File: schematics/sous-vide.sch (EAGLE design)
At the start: 31 parts, among them IC1 MEGA8-P, T1 BC547, T2 BC547, T3 BC547

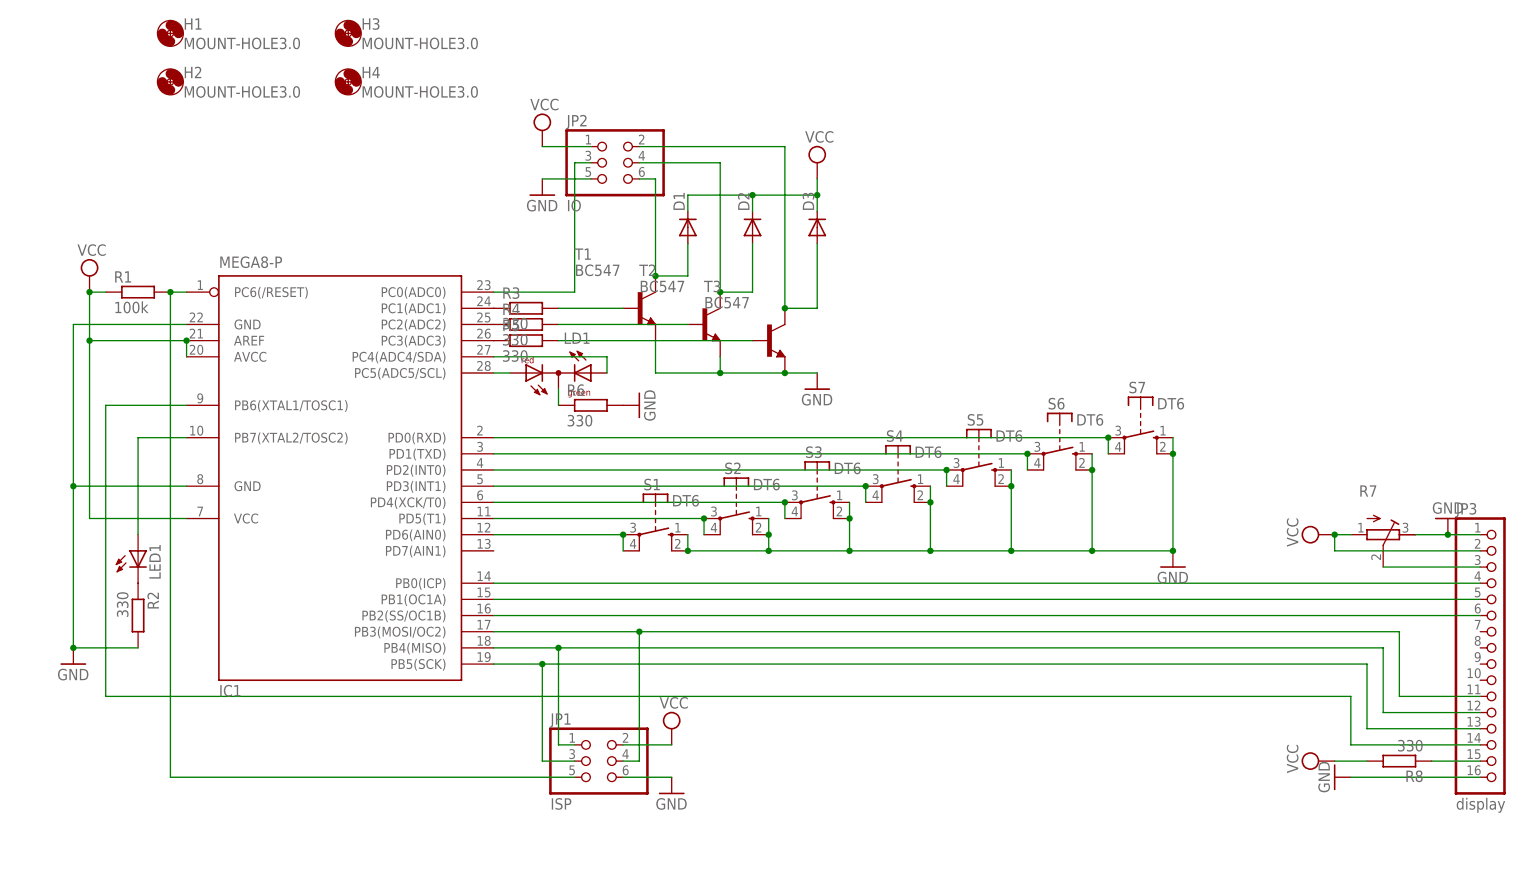
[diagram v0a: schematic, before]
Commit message: Reworked schema and pcb for new buttons and display.
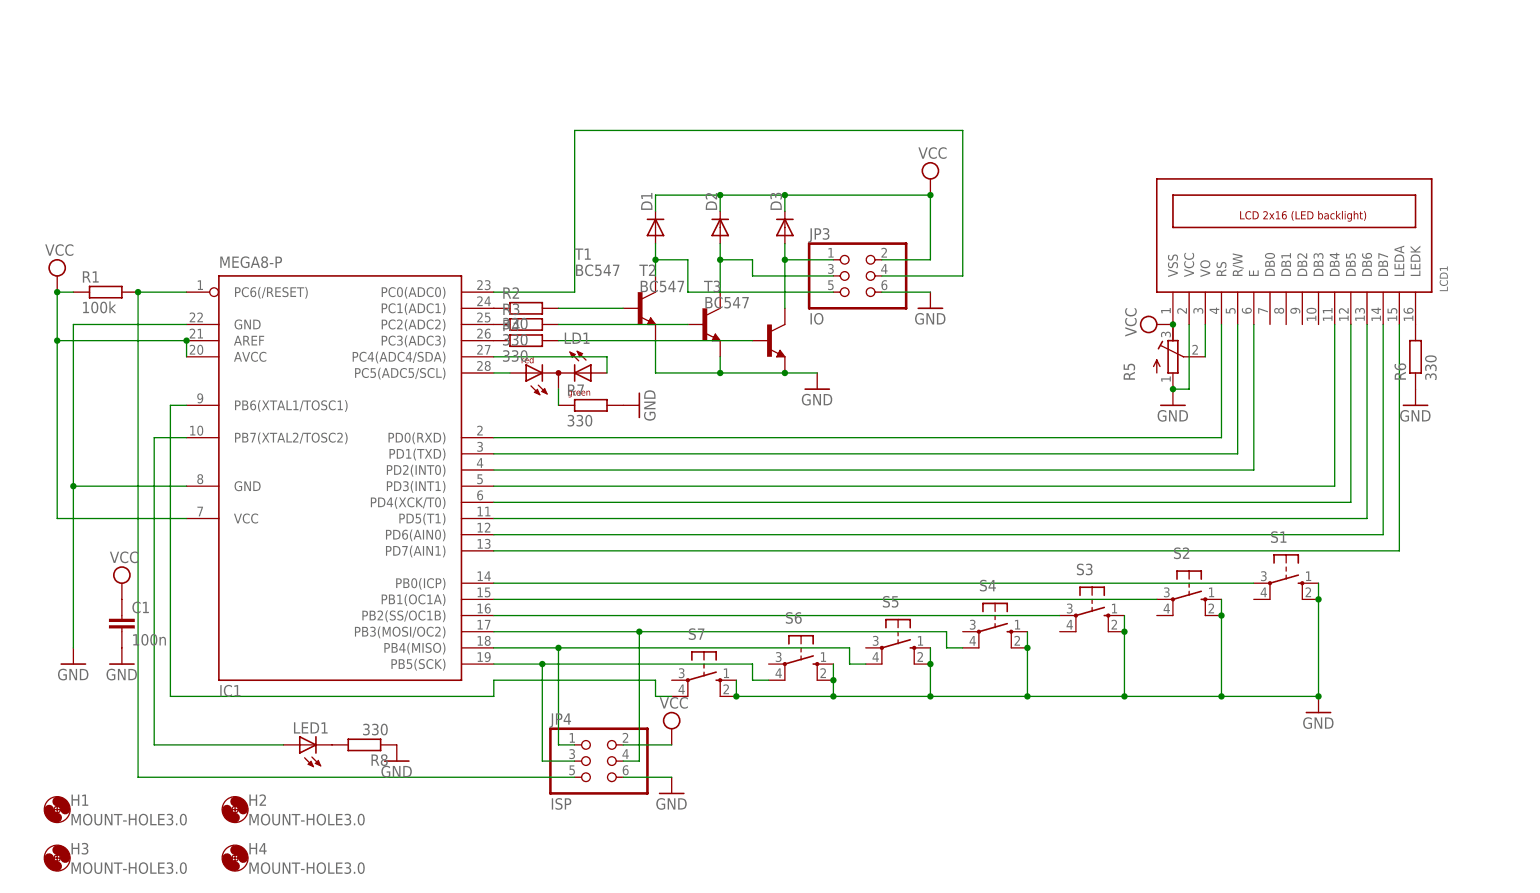
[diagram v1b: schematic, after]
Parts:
- removed JP2: IO, pinhead:PINHD-2X3
- added C1: 100n, resistor:C-EU025-025X050
- added LCD1: LCD_2X16_SIL, lcd_2x16_led_backlight:LCD_2X16_SIL
- JP3: value display -> IO; device pinhead:PINHD-1X16 -> pinhead:PINHD-2X3
- R5: value 330 -> (none); device rcl:R-EU_0207/2V -> resistor:R-TRIMM3339P
- R7: value (none) -> 330; device resistor:R-TRIMM3339P -> rcl:R-EU_0207/2V
- S1, S2, S3, S4, S5, S6, S7: value DT6 -> (none); device switch-misc:DT6 -> switch-omron:40-XX
- renumbered JP1 to JP4
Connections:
- removed net N$15 (its old number): JP3.15, R8.1
- removed net N$20: IC1.PB0(ICP), JP3.4
- new net N$2: LCD1.LEDK, R6.2
- new net N$33: IC1.PD6(AIN0), LCD1.DB7
- new net N$34: IC1.PD7(AIN1), LCD1.LEDA
- net GND: now also C1.2, JP3.6, LCD1.VCC, R5.E, R6.1, R7.2, R8.1, S1.S1, S2.S1, S3.S1, S4.S1, S5.S1, S6.S1, S7.S1; no longer JP2.5, JP3.1, JP3.16, R2.2, R6.2, R7.A, S1.S@1, S2.S@1, S3.S@1, S4.S@1, S5.S@1, S6.S@1, S7.S@1
- net N$1: now also R8.2; no longer R2.1
- net N$10: now also R2.2; no longer R3.2
- net N$11: now also R3.2; no longer R4.2
- net N$12: now also R4.2; no longer R5.2
- net N$13: now also JP3.5; no longer JP2.6
- net N$14: now also LCD1.VO, R5.S; no longer JP3.3, R7.S
- net N$16: now also JP3.3; no longer JP2.4
- net N$17: now also JP3.1; no longer JP2.2
- net N$18: now also S6.P1; no longer JP3.13
- net N$19: now also S5.P1; no longer JP3.12
- net N$21: now also IC1.PD0(RXD), LCD1.RS; no longer IC1.PB1(OC1A), JP3.5
- net N$22: now also IC1.PD1(TXD), LCD1.R/W; no longer IC1.PB2(SS/OC1B), JP3.6
- net N$23: now also IC1.PD2(INT0), LCD1.E; no longer IC1.PB6(XTAL1/TOSC1), JP3.14
- net N$24: now also S4.P1; no longer JP3.11
- net N$26: now also IC1.PB6(XTAL1/TOSC1), S7.P1; no longer IC1.PD6(AIN0), S1.P, S1.P@1
- net N$28: now also IC1.PD3(INT1), LCD1.DB4; no longer IC1.PD5(T1), S2.P, S2.P@1
- net N$3: now also JP3.4; no longer JP2.3
- net N$30: now also IC1.PD4(XCK/T0), LCD1.DB5; no longer IC1.PD3(INT1), S4.P, S4.P@1
- net N$32: now also IC1.PD5(T1), LCD1.DB6; no longer IC1.PD4(XCK/T0), S3.P, S3.P@1
- net N$35: now also IC1.PB2(SS/OC1B), S3.P; no longer IC1.PD2(INT0), S5.P, S5.P@1
- net N$36: now also IC1.PB0(ICP), S1.P; no longer IC1.PD0(RXD), S7.P, S7.P@1
- net N$37: now also IC1.PB1(OC1A), S2.P; no longer IC1.PD1(TXD), S6.P, S6.P@1
- net N$4: now also R2.1; no longer R3.1
- net N$5: now also R3.1; no longer R4.1
- net N$6: now also R4.1; no longer R5.1
- net N$7: now also R7.1; no longer R6.1
- net VCC: now also C1.1, LCD1.VSS, R5.A; no longer JP2.1, R7.E, R8.2
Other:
- moved on the sheet: D1, D2, D3, H1, H2, H3, H4, LED1, R1, R2, R3, R4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

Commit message: Minor tweaks before shipping to pcb manufacturer.
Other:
- moved on the sheet: LCD1, R5, R6
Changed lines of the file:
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@@
 <instance part="GND7" gate="1" x="5.08" y="33.02"/>
 <instance part="R7" gate="G$1" x="86.36" y="73.66"/>
-<instance part="GND5" gate="1" x="177.8" y="73.66"/>
-<instance part="R5" gate="G$1" x="177.8" y="81.28"/>
-<instance part="R6" gate="G$1" x="215.9" y="81.28" rot="R90"/>
-<instance part="SUPPLY4" gate="G$1" x="175.26" y="86.36" rot="R90"/>
-<instance part="GND6" gate="1" x="215.9" y="73.66"/>
+<instance part="GND5" gate="1" x="160.02" y="73.66"/>
+<instance part="R5" gate="G$1" x="160.02" y="81.28"/>
+<instance part="R6" gate="G$1" x="198.12" y="81.28" rot="R90"/>
+<instance part="SUPPLY4" gate="G$1" x="157.48" y="86.36" rot="R90"/>
+<instance part="GND6" gate="1" x="198.12" y="73.66"/>
 <instance part="H1" gate="G$1" x="2.54" y="10.16"/>
 <instance part="H3" gate="G$1" x="2.54" y="2.54"/>
@@
 <instance part="R4" gate="G$1" x="76.2" y="83.82"/>
 <instance part="JP3" gate="A" x="127" y="93.98"/>
-<instance part="LCD1" gate="G$1" x="177.8" y="99.06" rot="R90"/>
+<instance part="LCD1" gate="G$1" x="160.02" y="99.06" rot="R90"/>
 <instance part="GND9" gate="1" x="55.88" y="17.78"/>
 <instance part="S7" gate="1" x="104.14" y="30.48" rot="R270"/>
@@
 <pinref part="GND5" gate="1" pin="GND"/>
 <pinref part="LCD1" gate="G$1" pin="VCC"/>
-<wire x1="180.34" y1="86.36" x2="180.34" y2="76.2" width="0.1524" layer="91"/>
-<wire x1="180.34" y1="76.2" x2="177.8" y2="76.2" width="0.1524" layer="91"/>
-<junction x="177.8" y="76.2"/>
+<wire x1="162.56" y1="86.36" x2="162.56" y2="76.2" width="0.1524" layer="91"/>
+<wire x1="162.56" y1="76.2" x2="160.02" y2="76.2" width="0.1524" layer="91"/>
+<junction x="160.02" y="76.2"/>
 </segment>
 <segment>
@@
 <pinref part="SUPPLY4" gate="G$1" pin="VCC"/>
 <pinref part="R5" gate="G$1" pin="A"/>
-<junction x="177.8" y="86.36"/>
+<junction x="160.02" y="86.36"/>
 </segment>
 <segment>
@@
 <pinref part="IC1" gate="G$1" pin="PD0(RXD)"/>
 <pinref part="LCD1" gate="G$1" pin="RS"/>
-<wire x1="71.12" y1="68.58" x2="185.42" y2="68.58" width="0.1524" layer="91"/>
-<wire x1="185.42" y1="68.58" x2="185.42" y2="86.36" width="0.1524" layer="91"/>
+<wire x1="71.12" y1="68.58" x2="167.64" y2="68.58" width="0.1524" layer="91"/>
+<wire x1="167.64" y1="68.58" x2="167.64" y2="86.36" width="0.1524" layer="91"/>
 </segment>
 </net>
@@
 <pinref part="IC1" gate="G$1" pin="PD1(TXD)"/>
 <pinref part="LCD1" gate="G$1" pin="R/W"/>
-<wire x1="71.12" y1="66.04" x2="187.96" y2="66.04" width="0.1524" layer="91"/>
-<wire x1="187.96" y1="66.04" x2="187.96" y2="86.36" width="0.1524" layer="91"/>
+<wire x1="71.12" y1="66.04" x2="170.18" y2="66.04" width="0.1524" layer="91"/>
+<wire x1="170.18" y1="66.04" x2="170.18" y2="86.36" width="0.1524" layer="91"/>
 </segment>
 </net>
@@
 <pinref part="IC1" gate="G$1" pin="PD2(INT0)"/>
 <pinref part="LCD1" gate="G$1" pin="E"/>
-<wire x1="71.12" y1="63.5" x2="190.5" y2="63.5" width="0.1524" layer="91"/>
-<wire x1="190.5" y1="63.5" x2="190.5" y2="86.36" width="0.1524" layer="91"/>
+<wire x1="71.12" y1="63.5" x2="172.72" y2="63.5" width="0.1524" layer="91"/>
+<wire x1="172.72" y1="63.5" x2="172.72" y2="86.36" width="0.1524" layer="91"/>
 </segment>
 </net>
@@
 <segment>
 <pinref part="IC1" gate="G$1" pin="PD3(INT1)"/>
-<wire x1="71.12" y1="60.96" x2="203.2" y2="60.96" width="0.1524" layer="91"/>
+<wire x1="71.12" y1="60.96" x2="185.42" y2="60.96" width="0.1524" layer="91"/>
 <pinref part="LCD1" gate="G$1" pin="DB4"/>
-<wire x1="203.2" y1="60.96" x2="203.2" y2="86.36" width="0.1524" layer="91"/>
+<wire x1="185.42" y1="60.96" x2="185.42" y2="86.36" width="0.1524" layer="91"/>
 </segment>
 </net>
@@
 <segment>
 <pinref part="IC1" gate="G$1" pin="PD4(XCK/T0)"/>
-<wire x1="71.12" y1="58.42" x2="205.74" y2="58.42" width="0.1524" layer="91"/>
+<wire x1="71.12" y1="58.42" x2="187.96" y2="58.42" width="0.1524" layer="91"/>
 <pinref part="LCD1" gate="G$1" pin="DB5"/>
-<wire x1="205.74" y1="58.42" x2="205.74" y2="86.36" width="0.1524" layer="91"/>
+<wire x1="187.96" y1="58.42" x2="187.96" y2="86.36" width="0.1524" layer="91"/>
 </segment>
 </net>
@@
 <segment>
 <pinref part="IC1" gate="G$1" pin="PD5(T1)"/>
-<wire x1="71.12" y1="55.88" x2="208.28" y2="55.88" width="0.1524" layer="91"/>
+<wire x1="71.12" y1="55.88" x2="190.5" y2="55.88" width="0.1524" layer="91"/>
 <pinref part="LCD1" gate="G$1" pin="DB6"/>
-<wire x1="208.28" y1="55.88" x2="208.28" y2="86.36" width="0.1524" layer="91"/>
+<wire x1="190.5" y1="55.88" x2="190.5" y2="86.36" width="0.1524" layer="91"/>
 </segment>
 </net>
@@
 <segment>
 <pinref part="IC1" gate="G$1" pin="PD6(AIN0)"/>
-<wire x1="71.12" y1="53.34" x2="210.82" y2="53.34" width="0.1524" layer="91"/>
+<wire x1="71.12" y1="53.34" x2="193.04" y2="53.34" width="0.1524" layer="91"/>
 <pinref part="LCD1" gate="G$1" pin="DB7"/>
-<wire x1="210.82" y1="86.36" x2="210.82" y2="53.34" width="0.1524" layer="91"/>
+<wire x1="193.04" y1="86.36" x2="193.04" y2="53.34" width="0.1524" layer="91"/>
 </segment>
 </net>
@@
 <pinref part="IC1" gate="G$1" pin="PD7(AIN1)"/>
 <pinref part="LCD1" gate="G$1" pin="LEDA"/>
-<wire x1="71.12" y1="50.8" x2="213.36" y2="50.8" width="0.1524" layer="91"/>
-<wire x1="213.36" y1="50.8" x2="213.36" y2="86.36" width="0.1524" layer="91"/>
+<wire x1="71.12" y1="50.8" x2="195.58" y2="50.8" width="0.1524" layer="91"/>
+<wire x1="195.58" y1="50.8" x2="195.58" y2="86.36" width="0.1524" layer="91"/>
 </segment>
 </net>
@@
 <pinref part="R5" gate="G$1" pin="S"/>
 <pinref part="LCD1" gate="G$1" pin="VO"/>
-<wire x1="182.88" y1="81.28" x2="182.88" y2="86.36" width="0.1524" layer="91"/>
-</segment>
-</net>
+<wire x1="165.1" y1="81.28" x2="165.1" y2="86.36" width="0.1524" layer="91"/>
+</segment>
+</net>

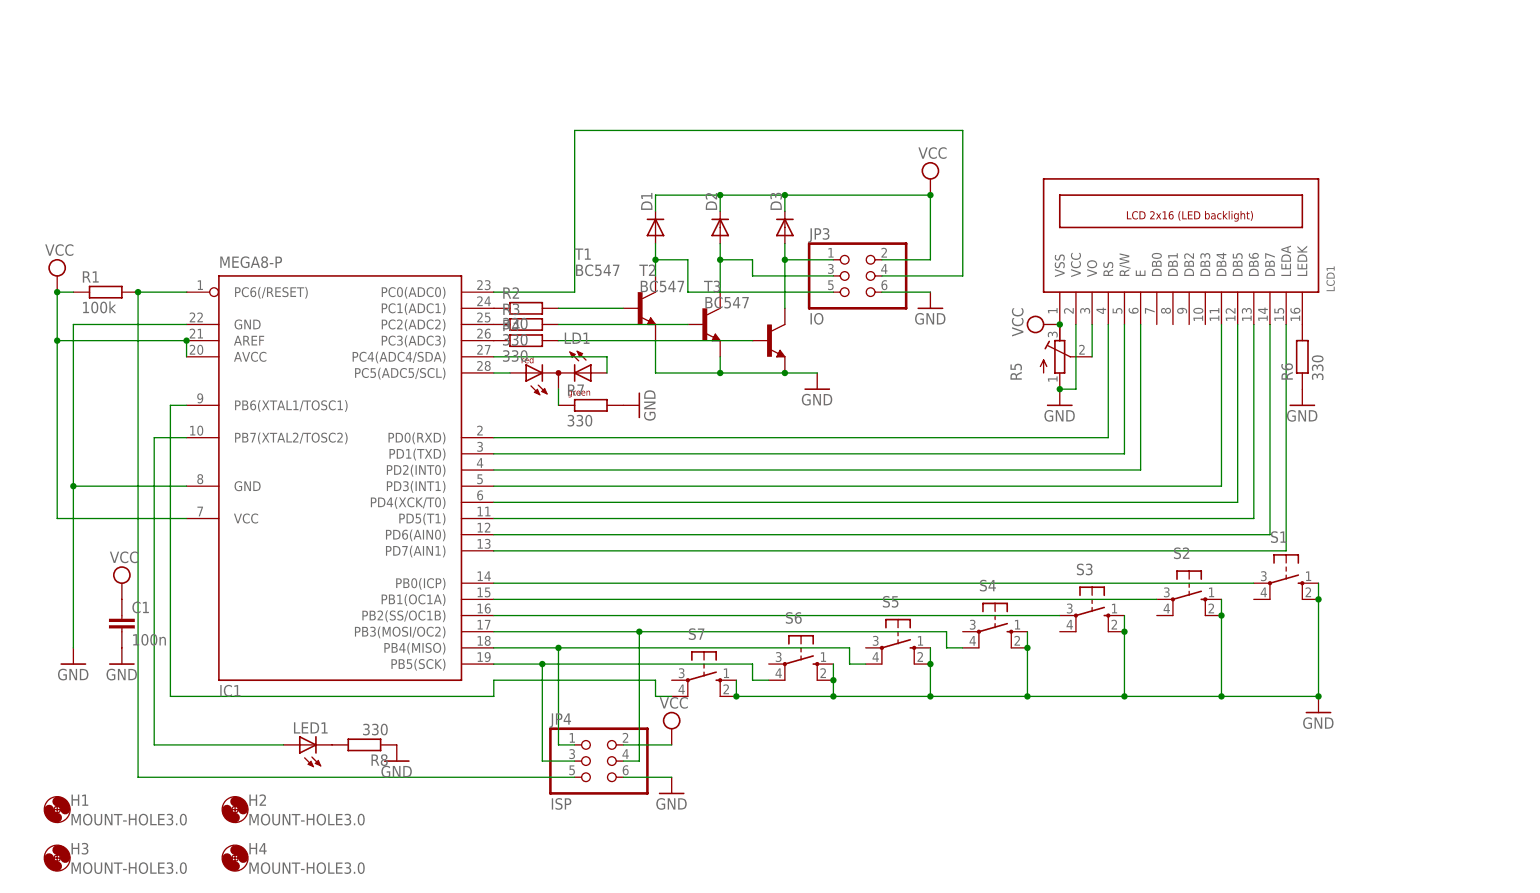
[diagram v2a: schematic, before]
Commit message: Fixed VCC/VDD/VSS/GND issue with display, renumbered parts, updated port assignment in code.
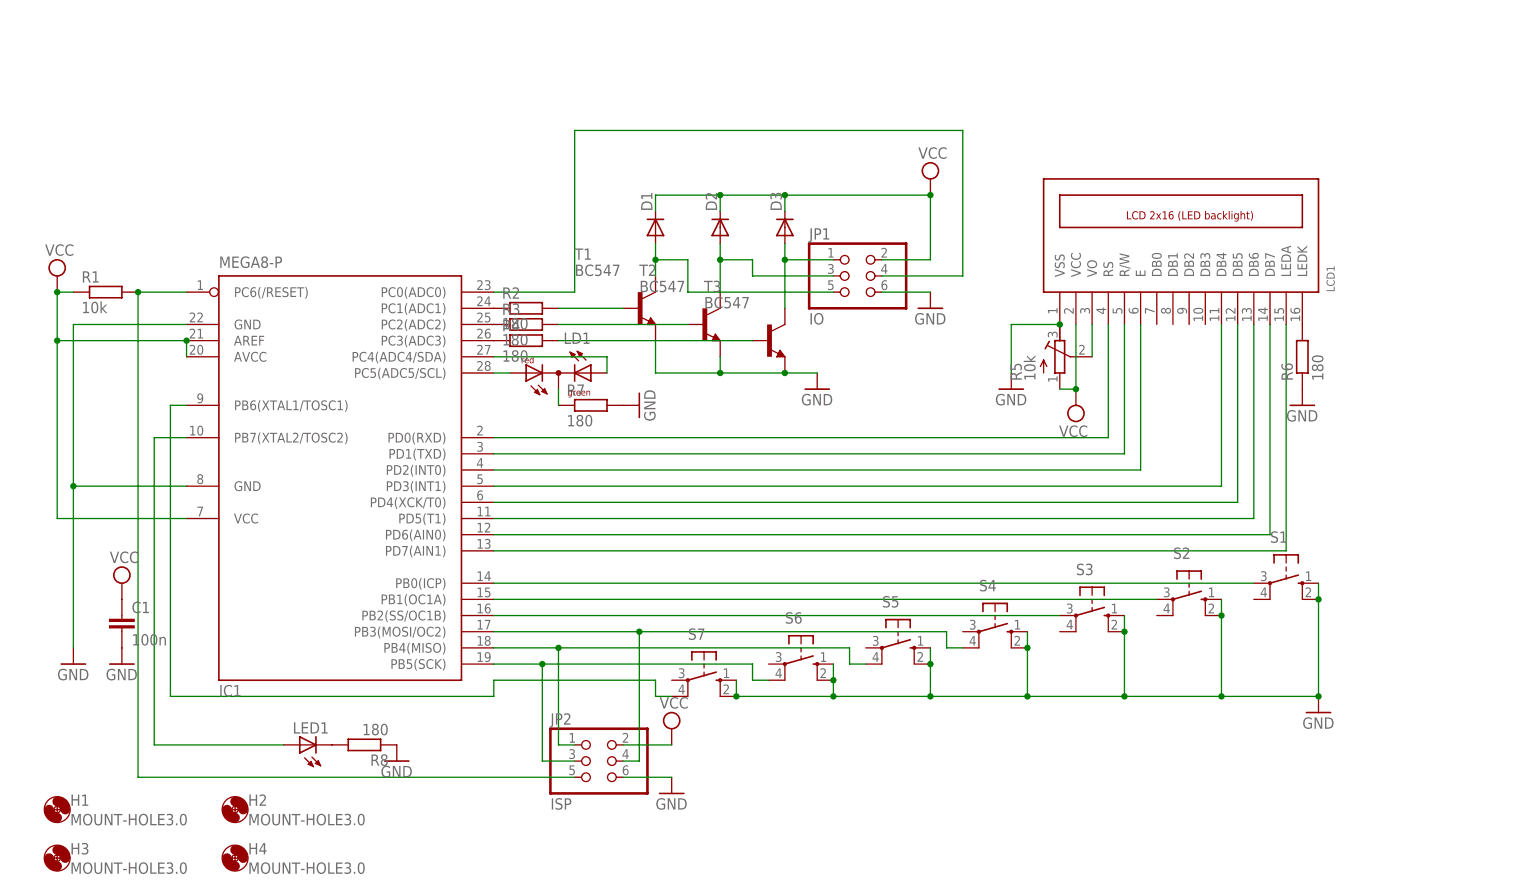
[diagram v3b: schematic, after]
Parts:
- R1: value 100k -> 10k
- R2, R3, R4, R6, R7, R8: value 330 -> 180
- R5: value (none) -> 10k
- renumbered JP3 to JP1, JP4 to JP2
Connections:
- net GND: now also LCD1.VSS, R5.A; no longer LCD1.VCC, R5.E
- net VCC: now also LCD1.VCC, R5.E; no longer LCD1.VSS, R5.A
